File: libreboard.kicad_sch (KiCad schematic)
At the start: 73 parts, among them J100 Screw Terminal, J101 Screw Terminal, J11 USB_C_Receptacle_USB2.0, J51 12V Fan 1, J52 12V Fan 2, J53 12V Fan 3, J54 12V Fan 4, U10 EMC2305-x-AP, U14 PTPS55289RYQR, U4 PTPS55289RYQR

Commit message: Re-save project in KiCad 10 format
Schematics and PCB were opened and saved with KiCad 10.0, which upgrades
the file format (PCB 20241229 -> 20260206, schematic 20250114 -> 20260306)
and adds KiCad 10 settings keys to the .kicad_pro.

No design changes: connectivity (netlist), tracks, vias, zones and all
194 footprint placements are identical to the previous commit.

Co-Authored-By: Claude Opus 5.5 <noreply@anthropic.com>
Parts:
- C26: now not fitted
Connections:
- net CC1 renamed CM5_GPIO ( Ethernet, GPIO, SDCARD)/CC1
- net CC2 renamed CM5_GPIO ( Ethernet, GPIO, SDCARD)/CC2
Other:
- note removed: "Check what to do with CC pins"

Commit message: Schematic: add missing libreboard: library prefix to six footprint links
J1, J6, J10, J17 (216989-0001_MOL) and U4, U14 (RYQ0021A-MFG) had
footprint fields without a library nickname, so KiCad could not resolve
them (ERC footprint_link_issues) and "Update PCB from Schematic" saw a
footprint change against the board, which already uses the
libreboard:-prefixed footprints. No connectivity change.

Co-Authored-By: Claude Opus 5.5 <noreply@anthropic.com>
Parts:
- U14, U4: footprint RYQ0021A-MFG -> libreboard:RYQ0021A-MFG
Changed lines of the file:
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@@
 			)
 		)
-		(property "Footprint" "RYQ0021A-MFG"
+		(property "Footprint" "libreboard:RYQ0021A-MFG"
 			(at 173.99 194.31 0)
 			(hide yes)
@@
 			)
 		)
-		(property "Footprint" "RYQ0021A-MFG"
+		(property "Footprint" "libreboard:RYQ0021A-MFG"
 			(at 177.8 306.07 0)
 			(hide yes)

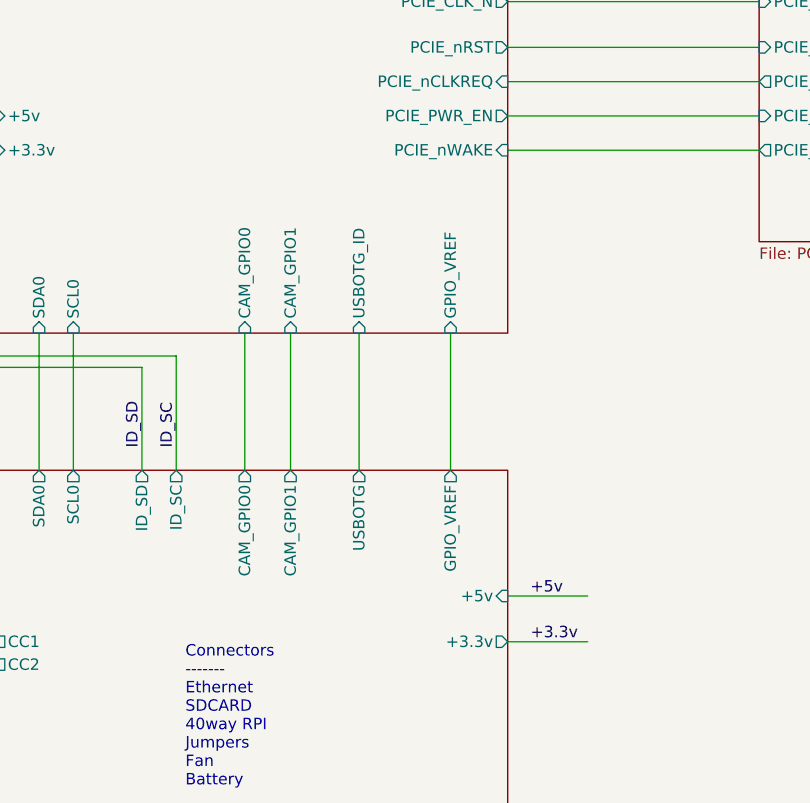
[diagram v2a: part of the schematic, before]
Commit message: USB hub: software-controlled hub reset from TCA9538 P7
The CM5 can now hard-reset the TUSB4041 hub over I2C, without
power-cycling anything else.

- U17 (TCA9538) P7 drives new net HUB_SW_RESETz into the manual-reset
  input (MR, pin 3) of the hub supervisor U19 (TPS3808G01). MR has an
  internal ~90k pull-up and the TCA9538 has no I/O pull-ups, so at
  power-up (P7 = input) the supervisor alone controls GRSTz as before.
- To reset: write 0 to P7 in the output register (0x01), then clear bit
  7 of the configuration register (0x03) so P7 drives low; after ~1 ms
  set the bit again. U19 holds GRSTz low while MR is low and for its
  20 ms timeout after release, so the hub always gets a valid (>= 3 ms)
  reset pulse regardless of software timing.
- U17 A0/A1 were floating; both now go to GND, fixing the expander at
  0x70 on i2c-0 (ID_SC/ID_SD), the address testscripts already use.
- Root sheet: HUB_SW_RESETz sheet pins on CM5_GPIO (out) and
  CM5_HighSpeed (in), wired like the other inter-sheet signals.

No new parts. PCB needs Update from Schematic and three short traces
(U17.12 to U19.3, U17.1 and U17.2 to GND). Netlist diff: only those
four pins change net. ERC 353 -> 348, only the U17 A0/A1/P7
unconnected warnings go away.

Refs #25.

Co-Authored-By: Claude Opus 5.5 <noreply@anthropic.com>
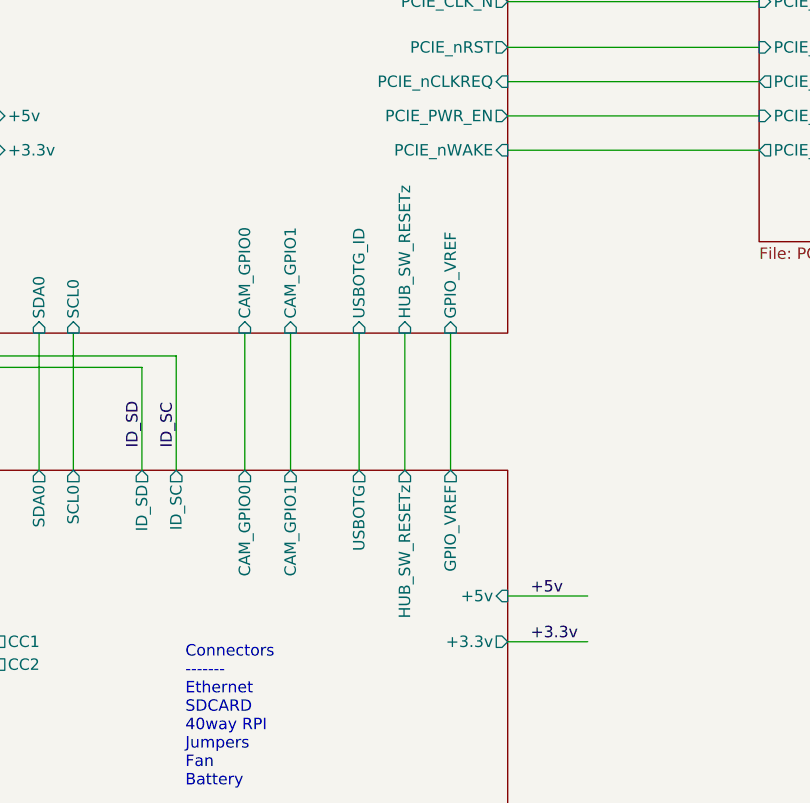
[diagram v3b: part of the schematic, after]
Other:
- sheet CM5_GPIO ( Ethernet, GPIO, SDCARD) ports: added HUB_SW_RESETz; removed none
- sheet CM5_HighSpeed ports: added HUB_SW_RESETz; removed none
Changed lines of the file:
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@@
 	(wire
 		(pts
+			(xy 175.26 96.52) (xy 175.26 111.76)
+		)
+		(stroke
+			(width 0)
+			(type default)
+		)
+	)
+	(wire
+		(pts
 			(xy 133.35 383.54) (xy 142.24 383.54)
 		)
@@
 			)
 		)
+		(pin "HUB_SW_RESETz" output
+			(at 175.26 111.76 90)
+			(effects
+				(font
+					(size 1.27 1.27)
+				)
+				(justify right)
+			)
+		)
 		(instances
 			(project "libreboard"
@@
 			(effects
 				(font
+					(size 1.27 1.27)
+				)
+				(justify left)
+			)
+		)
+		(pin "HUB_SW_RESETz" input
+			(at 175.26 96.52 270)
+			(effects
+				(font

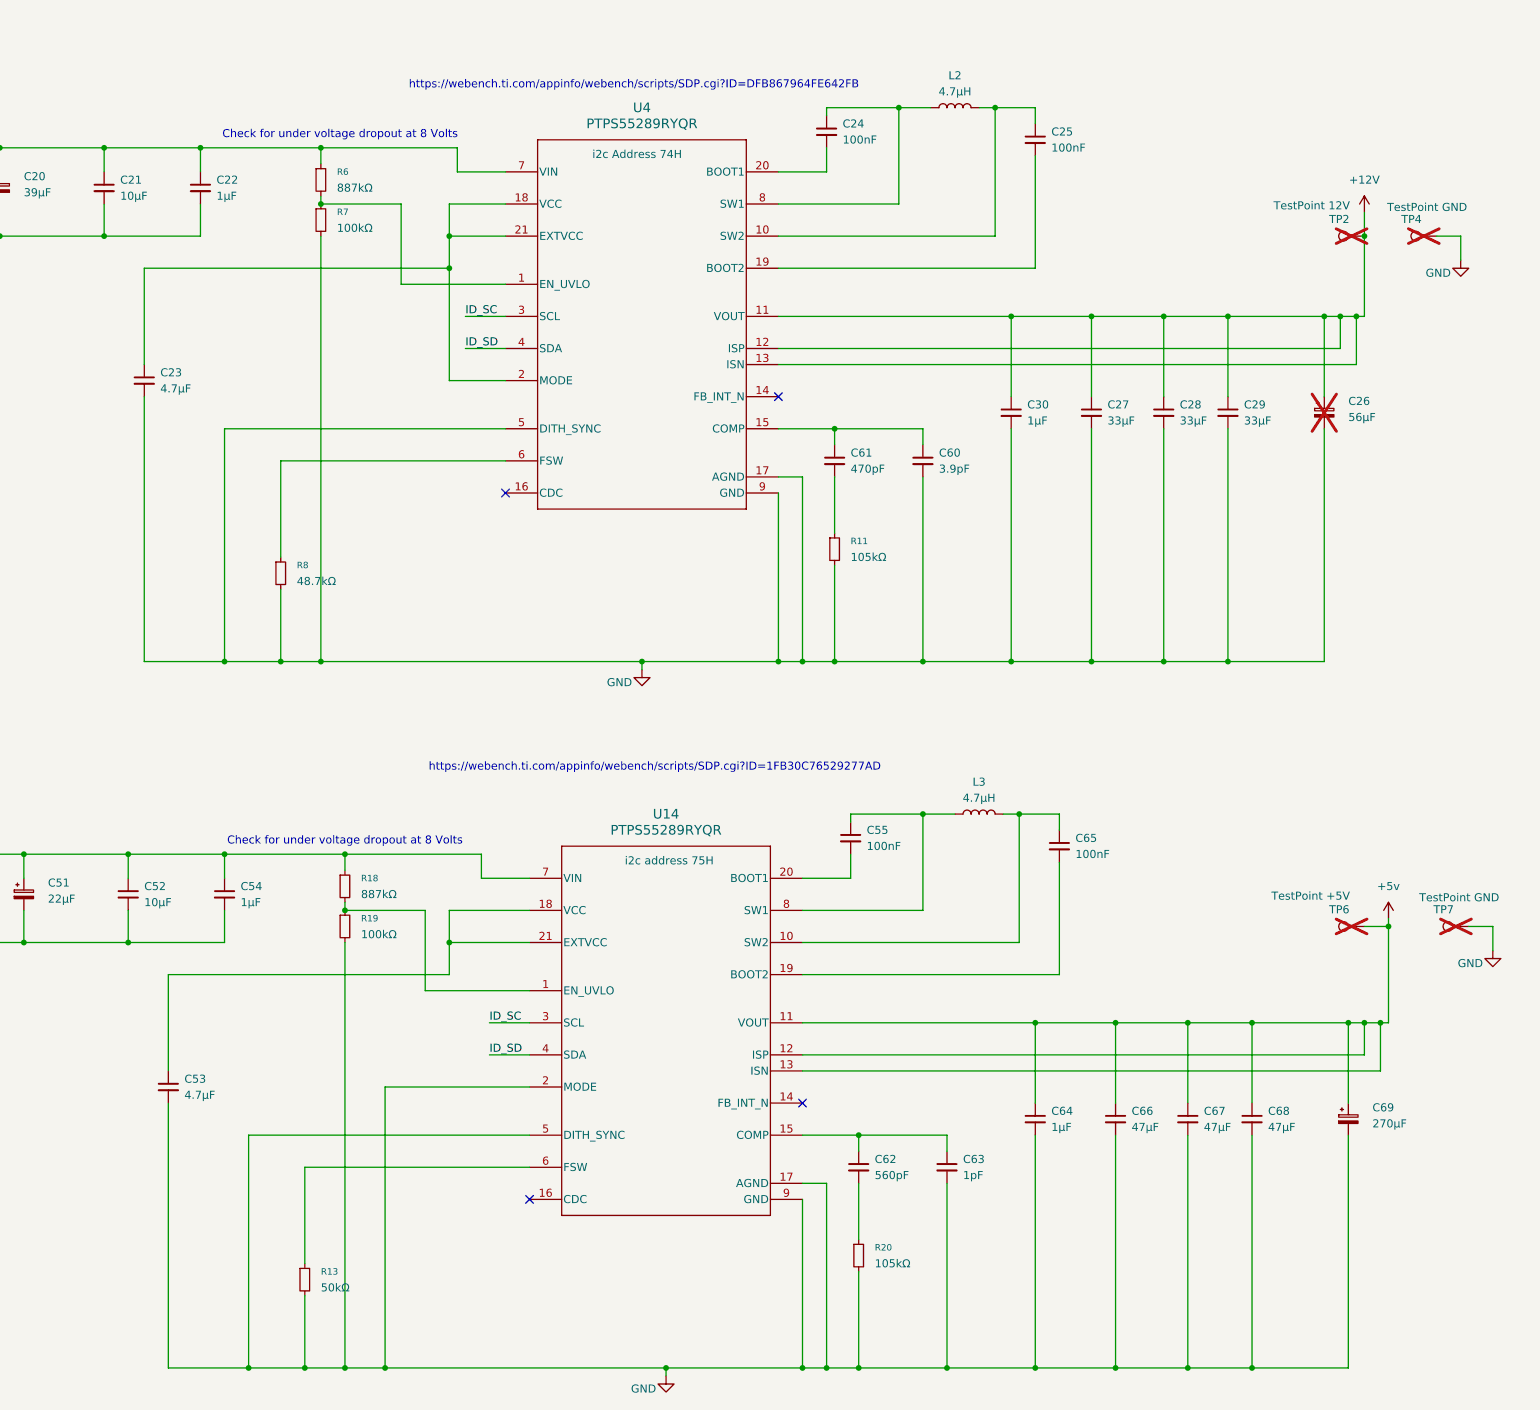
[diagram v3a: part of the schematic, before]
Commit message: Power: U4/U14 start on their own (TPS552892, resistor-set outputs)
The TPS55289 powers up with its output disabled (OE bit = 0) and needs
an I2C write to turn on. U14 makes the CM5's +5v, so the CM5 could
never send that write itself; Rev1 boards are jump-started by a Pico
on the 40-pin header. U4 (+12V for the fans) also waited for software.

Both become the TPS552892RYQR: the non-I2C variant in the same 21-pin
RYQ package with the same power, FSW, COMP, EN/UVLO and CDC pins. It
soft-starts (2.5-5 ms) as soon as EN/UVLO is above threshold.

- New symbol TPS55289:TPS552892RYQR (copy of PTPS55289RYQR with pins
  3/4/14 renamed PG/CC/FB).
- Pins 3/4 (PG/CC, open-drain on the new part) are taken off the
  ID_SC/ID_SD bus and marked no-connect.
- FB dividers, VREF 1.2 V: U14 R53 100k / R54 30.1k = 5.19 V;
  U4 R55 100k / R56 11.0k = 12.11 V.
- U14 MODE moves from GND to its VCC (forced PWM, as the Pico set it);
  U4 MODE was already on VCC.
- Compensation rescaled for the external divider (loop gain goes with
  VREF/VOUT; same 190 uA/V error amp and 55 mOhm sense in both parts):
  U14 R20 105k->25.5k, C62 560p->2.2n, C63 1p->3.9p (x4.1);
  U4 R11 105k->60.4k, C61 470p->1n, C60 3.9p->6.8p (x1.76).
- UVLO for a 12-24 V input: R18/R6 887k->301k, R19/R7 100k->45.3k,
  so both start at 9.4 V and drop out at 7.9 V (5 uA hysteresis
  current); the old divider needed 12.14 V to start. Sheet notes
  updated.
- C30 on +12V: 6.3 V part -> 50 V GRM155R61H105KE05D (already in BOM).

Netlist: only the listed pins, values and the four new resistors
change. ERC 348 -> 346 (remaining new entries are the usual
"unspecified pin type" warnings of this symbol). Digikey numbers
follow the existing Panasonic/Kyocera patterns and were not checked
live; left blank for GRM1555C1H102JA01D (C61) and 04025A6R8CAT2A (C60).

Co-Authored-By: Claude Opus 5.5 <noreply@anthropic.com>
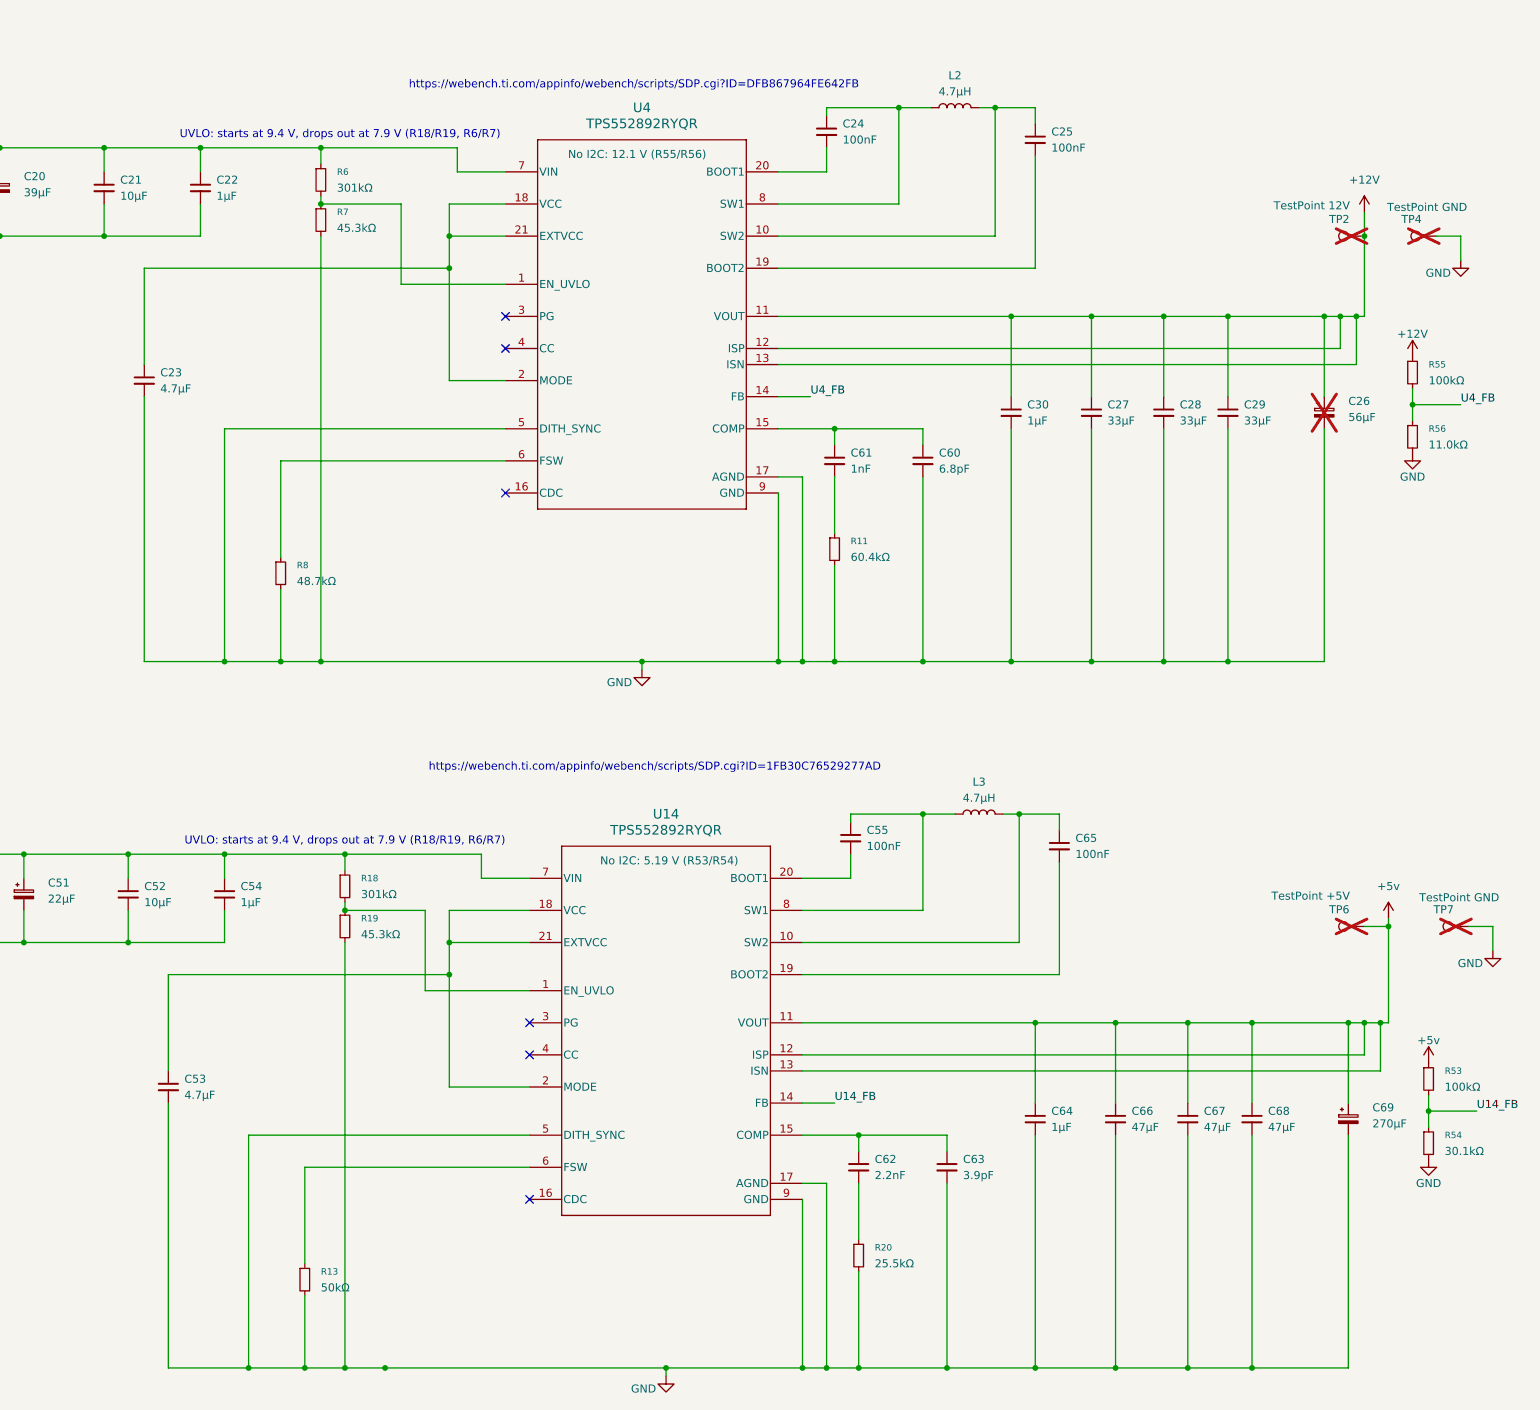
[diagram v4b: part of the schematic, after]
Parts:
- added R53, R55: 100kΩ, Resistor_SMD:R_0402_1005Metric, symbol Device:R_Small
- added R54: 30.1kΩ, Resistor_SMD:R_0402_1005Metric, symbol Device:R_Small
- added R56: 11.0kΩ, Resistor_SMD:R_0402_1005Metric, symbol Device:R_Small
- C30: Dist. P/N 478-KGM05AR50J105KHTR-ND -> 490-GRM155R61H105KE05DTR-ND; Manf. P/N 04026D105KAT2A -> GRM155R61H105KE05D; Manufacturer Kyocera -> Murata Electronics; Part Description Capacitor, Ceramic, 1µF, ±10%, 6.3V, X5R, 0402 (1005m) -> 1 µF ±10% 50V Ceramic Capacitor X5R 0402 (1005 Metric)
- C60: value 3.9pF -> 6.8pF; Dist. P/N 478-KGM05ACG1H3R9BHTR-ND -> (none); Manf. P/N KGM05ACG1H3R9BH -> 04025A6R8CAT2A; Part Description Capacitor, Ceramic, 3.9pF, ±2.5%, 50V, C0G/NP0, 0402 (1005m) -> Capacitor, Ceramic, 6.8pF, ±0.25pF, 50V, C0G/NP0, 0402 (100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
- C61: value 470pF -> 1nF; Dist. P/N 478-KGM05AR71H471KHTR-ND -> (none); Manf. P/N KGM05AR71H471KH -> GRM1555C1H102JA01D; Manufacturer Kyocera -> Murata Electronics; Part Description Capacitor, Ceramic, 470pF, ±10%, 50V, X7R, 0402 (1005m) -> Capacitor, Ceramic, 1nF, ±5%, 50V, C0G/NP0, 0402 (1005m)
- C62: value 560pF -> 2.2nF; Dist. P/N 478-1098-2-ND -> 478-KGM05AR71H222KHTR-ND; Manf. P/N 04025C561KAT2A -> KGM05AR71H222KH; Part Description Capacitor, Ceramic, 560pF, ±10%, 50V, X7R, 0402 (1005m) -> Capacitor, Ceramic, 2.2nF, ±10%, 50V, X7R, 0402 (1005m)
- C63: value 1pF -> 3.9pF; Dist. P/N 478-KGQ05FCG1H1R0BHTR-ND -> 478-KGM05ACG1H3R9BHTR-ND; Manf. P/N 04025U1R0BAT2A -> KGM05ACG1H3R9BH; Part Description Capacitor, Ceramic, 1pF, ±10%, 50V, C0G/NP0, 0402 (1005m) -> Capacitor, Ceramic, 3.9pF, ±2.5%, 50V, C0G/NP0, 0402 (1005m)
- R11: value 105kΩ -> 60.4kΩ; Dist. P/N P105KLTR-ND -> P60.4KLTR-ND; Manf. P/N ERJ-2RKF1053X -> ERJ-2RKF6042X; Part Description Resistor, 105kΩ, ±1%, 0.1W, SMD 0402 (1005m) -> Resistor, 60.4kΩ, ±1%, 0.1W, SMD 0402 (1005m)
- R18, R6: value 887kΩ -> 301kΩ; Dist. P/N P887KLTR-ND -> P301KLTR-ND; Manf. P/N ERJ-2RKF8873X -> ERJ-2RKF3013X; Part Description Resistor, 887kΩ, ±1%, 0.1W, SMD 0402 (1005m) -> Resistor, 301kΩ, ±1%, 0.1W, SMD 0402 (1005m)
- R19, R7: value 100kΩ -> 45.3kΩ; Dist. P/N 10-ERJ-U02F1003XTR-ND -> P45.3KLTR-ND; Manf. P/N ERJ-U02F1003X -> ERJ-2RKF4532X; Part Description Resistor, 100kΩ, ±1%, 0.1W, SMD 0402 (1005m) -> Resistor, 45.3kΩ, ±1%, 0.1W, SMD 0402 (1005m)
- R20: value 105kΩ -> 25.5kΩ; Dist. P/N P105KLTR-ND -> P25.5KLTR-ND; Manf. P/N ERJ-2RKF1053X -> ERJ-2RKF2552X; Part Description Resistor, 105kΩ, ±1%, 0.1W, SMD 0402 (1005m) -> Resistor, 25.5kΩ, ±1%, 0.1W, SMD 0402 (1005m)
- U14, U4: value PTPS55289RYQR -> TPS552892RYQR; symbol TPS55289:PTPS55289RYQR -> TPS55289:TPS552892RYQR; Dist. P/N 296-TPS55289RYQRTR-ND -> 296-TPS552892RYQRTR-ND; Manf. P/N TPS55289RYQR -> TPS552892RYQR; Part Description IC, Buck Boost, 0.8v, 1-output, 8A -> IC, Buck Boost, 0.8-22V, 1-output, 8A, external feedback, n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
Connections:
- net +12V: now also R55.1
- net +5v: now also R53.1
- net GND: now also R54.2, R56.2; no longer U14.2 (MODE)
- net ID_SC: no longer U14.3 (SCL), U4.3 (SCL)
- net ID_SD: no longer U14.4 (SDA), U4.4 (SDA)
- net U4_FB: now reaches U4.14 (FB)
- net U4_FB: now also R55.2, R56.1
- net at C53.1, U14.18 (VCC), U14.21 (EXTVCC): now also U14.2 (MODE)
- net U14_FB: now reaches U14.14 (FB)
- net U14_FB: now also R53.2, R54.1
- no-connect marks 7 -> 9
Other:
- note added: "UVLO: starts at 9.4 V, drops out at 7.9 V (R18/R19, R6/R7)"
- note removed: "Check for under voltage dropout at 8 Volts"
